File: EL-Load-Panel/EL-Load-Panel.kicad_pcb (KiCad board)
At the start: 2 copper layers, 127 x 53 mm, 40 parts, among them J1 Touchscreen, J2 Conn_02x08_Odd_Even, SW1 ON/OFF, U1 MCP23008-xSO

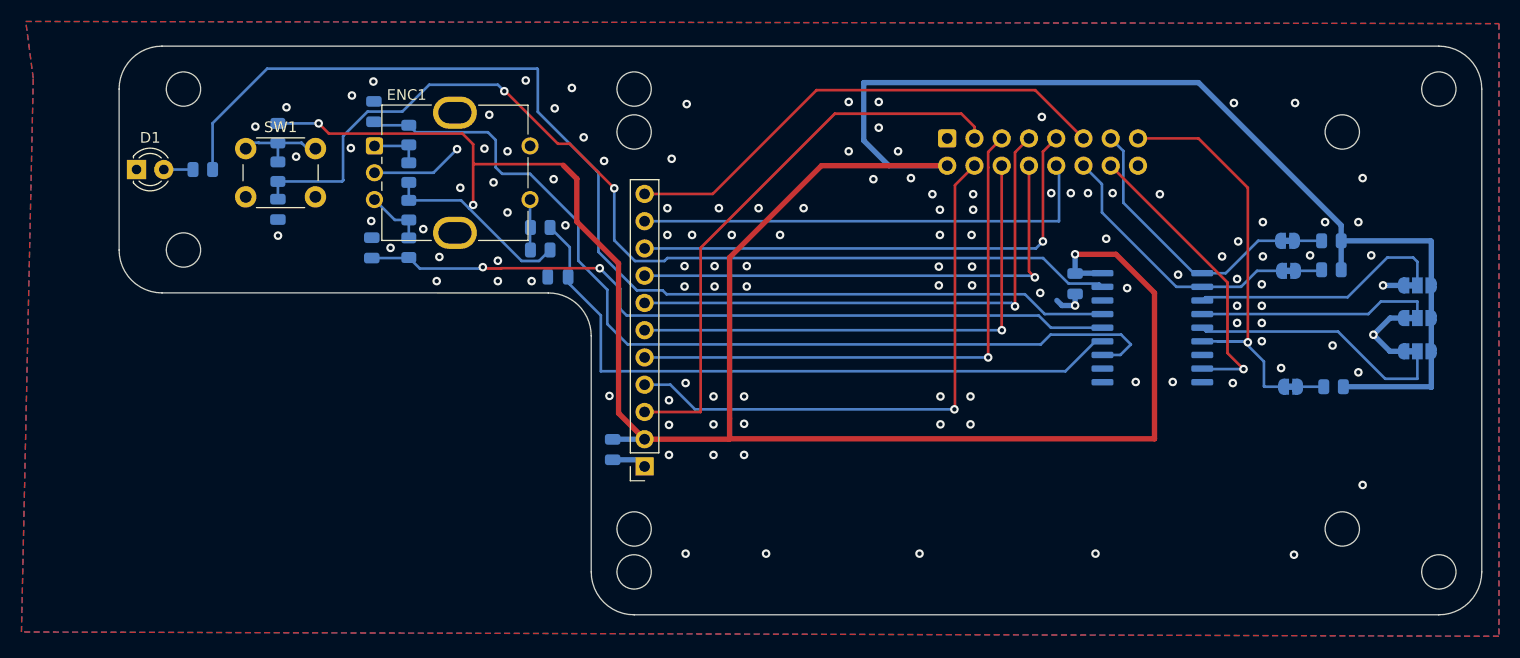
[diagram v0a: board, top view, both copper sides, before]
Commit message: Added extra capacitor to Panel for stability. Upped schematic and pcb revisions to v2r3.
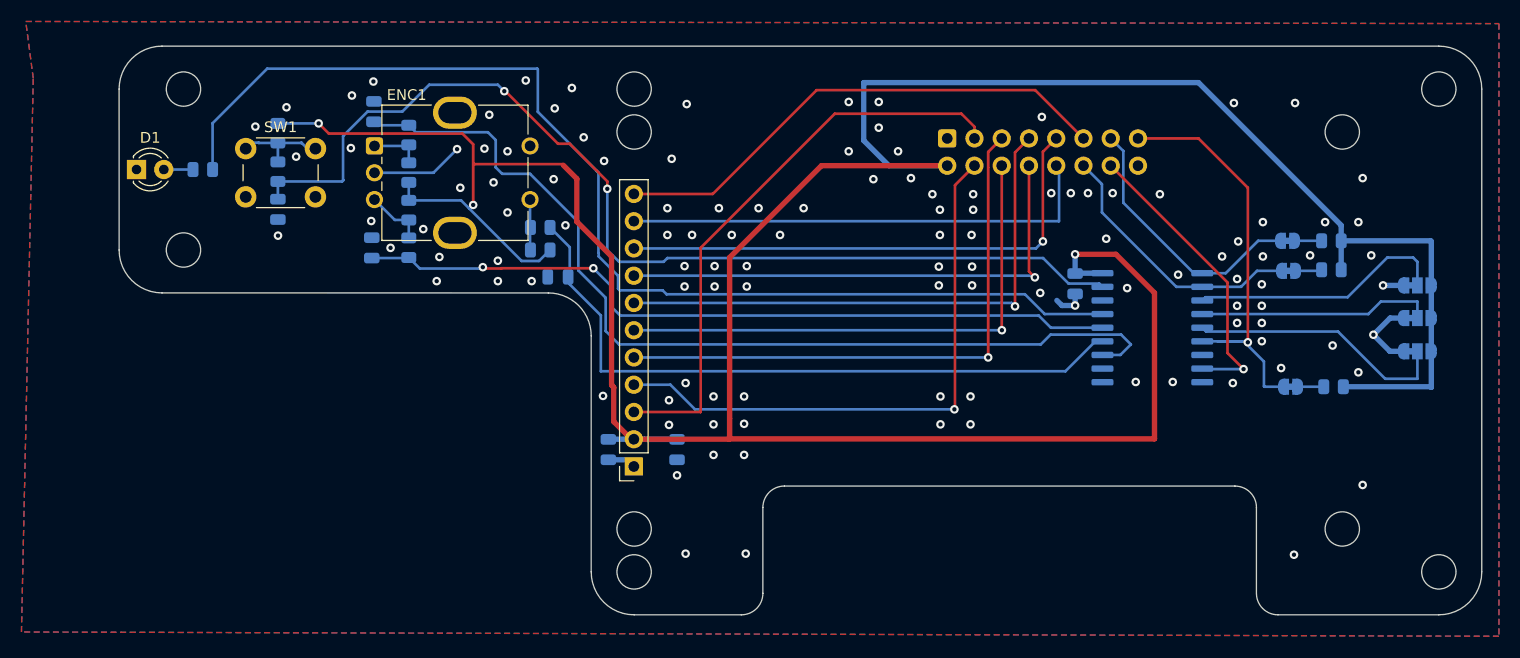
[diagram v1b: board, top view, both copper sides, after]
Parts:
- added C6: 10u, Capacitor_SMD:C_0805_2012Metric, B.Cu at (174.1, 98.8)
- moved J1 1.00 mm to (170.1, 100.4)
- moved C1 0.40 mm to (167.7, 98.8)
- renumbered locked to H1
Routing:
- net +3V3: track 296.6 -> 300.7 mm
- net /SCLK: track 52.8 -> 53.8 mm
- net /RESET: track 53.0 -> 54.0 mm
- net /PEN: track 46.8 -> 47.8 mm
- net /MOSI: track 53.3 -> 54.3 mm
- net /MISO: track 47.1 -> 48.1 mm
- net /DC: track 48.7 -> 49.7 mm
- net /CS2: track 44.3 -> 45.3 mm
- net /CS1: track 47.5 -> 48.5 mm
- net /BLK: track 50.8 -> 51.8 mm
- net /sw0: track 95.6 -> 96.5 mm
- net /sw4: track 105.8 -> 106.7 mm
- net GND: track 23.6 -> 23.1 mm, vias 120 -> 118
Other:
- outline, holes or cut-outs redrawn
- board text added: "${TITLE} ${REVISION} ${ISSUE_DATE}"
- board text removed: "locked"

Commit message: Initial Panel v3 commit
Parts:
- added C10: 100n, Capacitor_SMD:C_0805_2012Metric, B.Cu at (137.7, 82.7)
- added C8: 10u, Capacitor_SMD:CP_Elec_5x5.8, F.Cu at (183.2, 95.5)
- added C9: 100n, Capacitor_SMD:C_0805_2012Metric, B.Cu at (192.4, 71.4)
- added J3: Conn_01x04_Socket, Connector_Phoenix_MC:PhoenixContact_MCV_1,5_4-G-3.81_1x04_P3.81mm_Vertical, F.Cu at (127.3, 88.7)
- added U2: USBLC6-2SC6, Package_TO_SOT_SMD:SOT-23-6, B.Cu at (133.9, 81.5)
- C6: footprint Capacitor_SMD:C_0805_2012Metric -> Capacitor_SMD:CP_Elec_5x5.8
- moved C6 31.3 mm to (188.0, 70.8), turned to 90 degrees
- moved C1 0.20 mm to (167.5, 98.8)
- moved J1 0.20 mm to (169.9, 100.4)
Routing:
- net /SDA: track 25.3 -> 136.1 mm, vias 0 -> 1
- net /SCL: track 25.3 -> 135.2 mm, vias 0 -> 1
- net +3V3: track 300.7 -> 359.3 mm, vias 3 -> 4
- net Net-(J3-Pin_2): track 0.00 -> 6.83 mm
- net Net-(J3-Pin_3): track 0.00 -> 6.09 mm
- net GND: track 23.1 -> 28.3 mm, vias 118 -> 153
- net /MOSI: track 54.3 -> 51.4 mm
- net /sw4: track 106.7 -> 104.1 mm
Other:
- outline, holes or cut-outs redrawn
- board text added: "GND"
- board text added: "SCL SDA 3V3"
